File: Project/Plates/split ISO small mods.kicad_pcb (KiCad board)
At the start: 2 copper layers, 257.2 x 76.2 mm, 47 parts

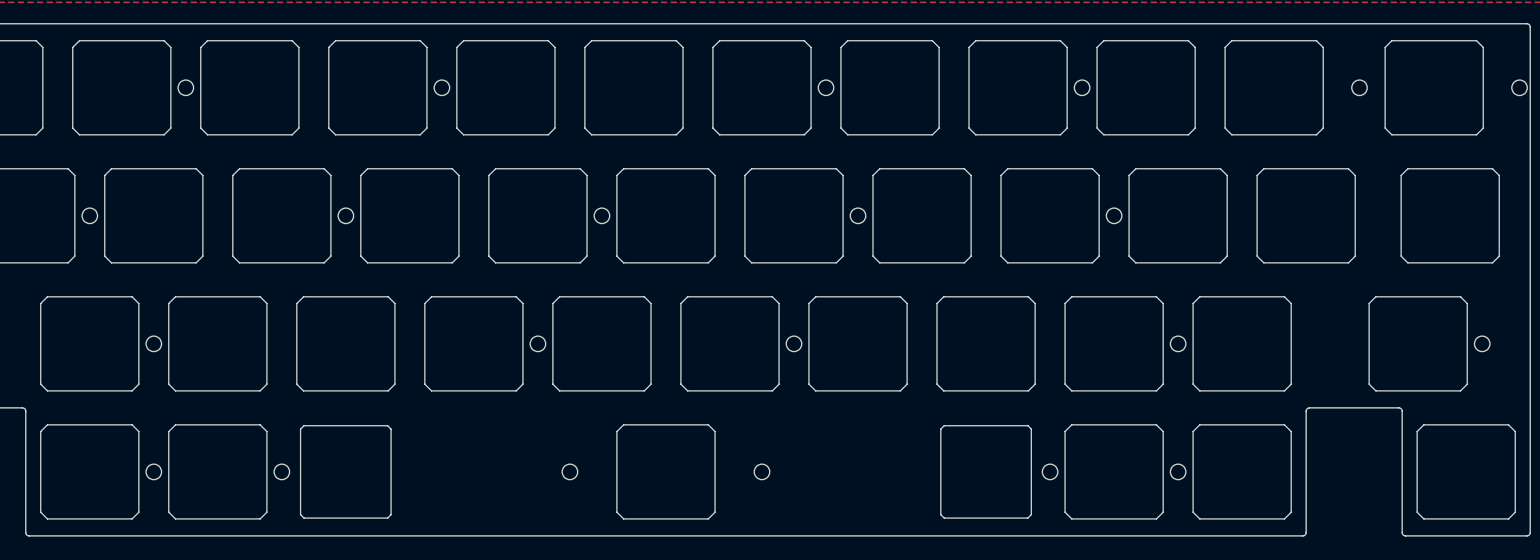
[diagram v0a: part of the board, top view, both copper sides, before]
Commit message: bottom row change, plate update, firmware update
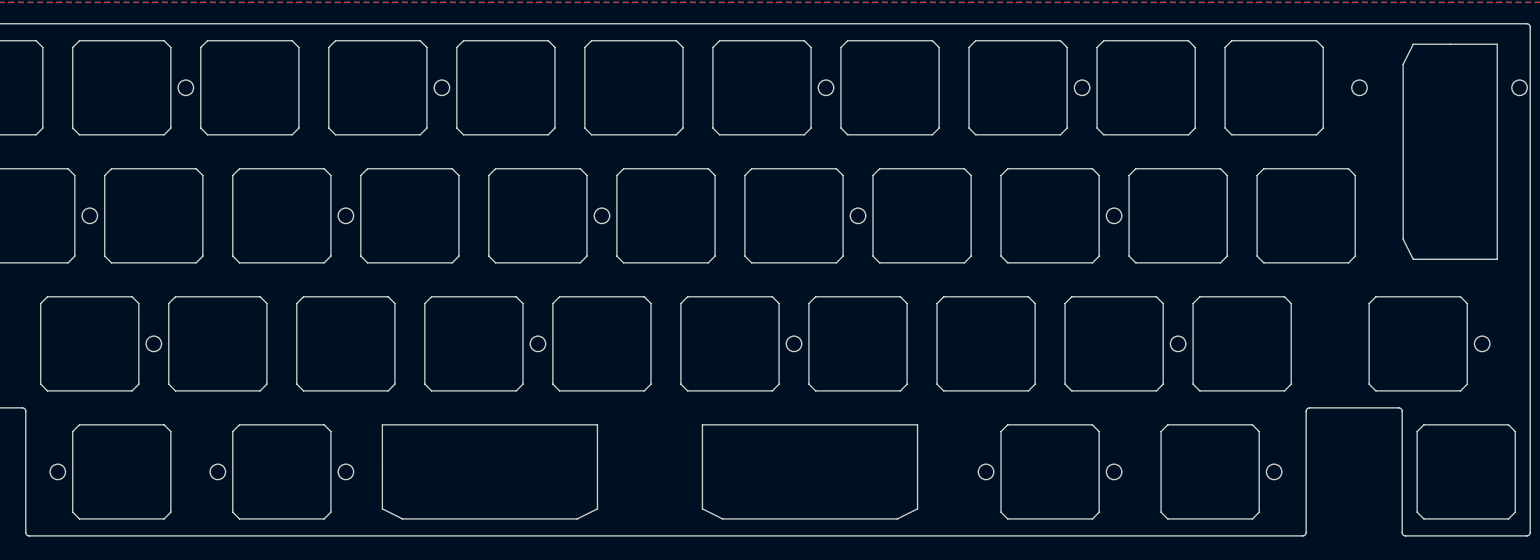
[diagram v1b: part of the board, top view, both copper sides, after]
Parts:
- removed the REF** at (146.1, 91.3) (x3)
- removed the REF** at (231.8, 91.3)
- removed the REF** at (79.4, 91.3)
- removed the REF** at (60.3, 91.3)
- removed the REF** at (262.7, 53.2)
- removed the REF** at (212.7, 91.3)
- removed the REF** at (260.4, 34.1)
- added REF**: Value, cipulot_parts:ecs_plate_cut_1U, F.Cu at (227.0, 91.3)
- added REF**: Value, cipulot_parts:ecs_plate_cut_2U, F.Cu at (167.5, 91.3)
- added REF**: Value, cipulot_parts:ecs_plate_cut_1U, F.Cu at (88.9, 91.3)
- added REF**: Value, cipulot_parts:ecs_plate_cut_1U, F.Cu at (203.2, 91.3)
- added REF**: Value, cipulot_parts:ecs_plate_cut_2U, F.Cu at (262.7, 43.7)
- added REF**: Value, cipulot_parts:ecs_plate_cut_1U, F.Cu at (65.1, 91.3)
- added REF**: Value, cipulot_parts:ecs_plate_cut_2U, F.Cu at (119.9, 91.3)
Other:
- outline, holes or cut-outs redrawn
- board text removed: "REF**"
